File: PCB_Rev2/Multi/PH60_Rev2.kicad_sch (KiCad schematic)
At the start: 28 parts, among them J1 USB_C_Receptacle_USB2.0_16P, J2 Conn_01x02, U1 TLV1117-33, U2 W25Q128JVS, U3 RP2040, Y1 Crystal_GND24

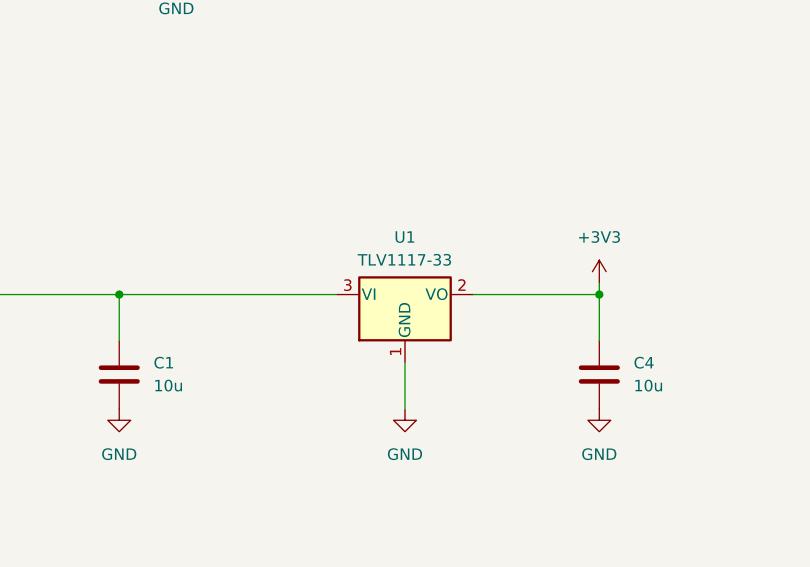
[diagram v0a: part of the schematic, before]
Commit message: LDO Modification
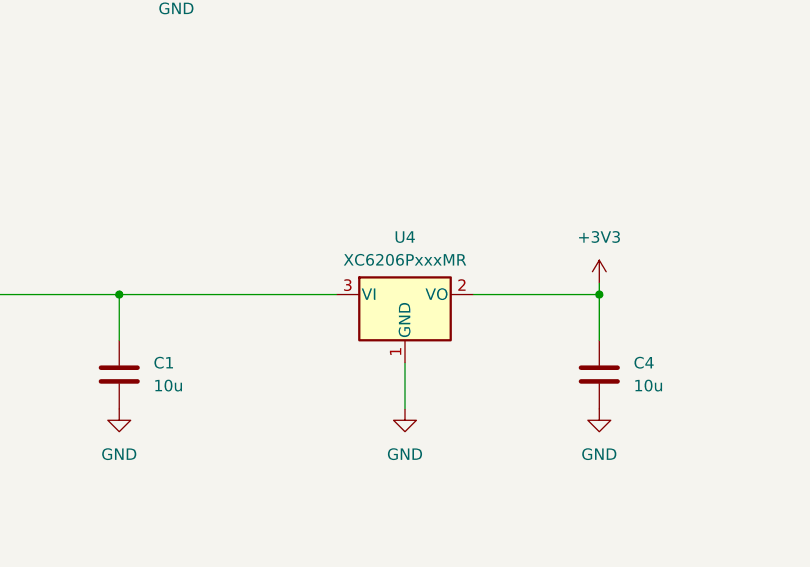
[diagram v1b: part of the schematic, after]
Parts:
- removed U1: TLV1117-33, Package_TO_SOT_SMD:SOT-89-3_Handsoldering, symbol Regulator_Linear:TLV1117-33
- added U4: XC6206PxxxMR, Package_TO_SOT_SMD:SOT-23-3, symbol Regulator_Linear:XC6206PxxxMR
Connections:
- net +3V3: now also U4.2 (VO)
- net GND: now also U4.1 (GND)
- net VBUS: now also U4.3 (VI)
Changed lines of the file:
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@@
-	)
-	(symbol
-		(lib_id "Regulator_Linear:TLV1117-33")
-		(at 134.62 196.85 0)
-		(unit 1)
-		(exclude_from_sim no)
-		(in_bom yes)
-		(on_board yes)
-		(dnp no)
-		(fields_autoplaced yes)
-		(property "Reference" "U1"
-			(at 134.62 190.5 0)
-			(effects
-				(font
-					(size 1.27 1.27)
-				)
-			)
-		)
-		(property "Value" "TLV1117-33"
-			(at 134.62 193.04 0)
-			(effects
-				(font
-					(size 1.27 1.27)
-				)
-			)
-		)
-		(property "Footprint" "Package_TO_SOT_SMD:SOT-89-3_Handsoldering"
-			(at 134.62 196.85 0)
-			(effects
-				(font
-					(size 1.27 1.27)
-				)
-				(hide yes)
-			)
-		)
-		(property "Datasheet" "http://www.ti.com/lit/ds/symlink/tlv1117.pdf"
-			(at 134.62 196.85 0)
-			(effects
-				(font
-					(size 1.27 1.27)
-				)
-				(hide yes)
-			)
-		)
-		(property "Description" "800mA Low-Dropout Linear Regulator, 3.3V fixed output, TO-220/TO-252/TO-263/SOT-223"
-			(at 134.62 196.85 0)
-			(effects
-				(font
-					(size 1.27 1.27)
-				)
-				(hide yes)
-			)
-		)
-		(pin "3"
-		)
-		(pin "1"
-		)
-		(pin "2"
-		)
-		(instances
-			(project ""
-				(path "/dca0f898-8fdb-4522-a51d-f4f4238906e7"
-					(reference "U1")
-					(unit 1)
-				)
-			)
-		)
 	)
 	(symbol
@@
 	)
 	(symbol
+		(lib_id "Regulator_Linear:XC6206PxxxMR")
+		(at 134.62 196.85 0)
+		(unit 1)
+		(exclude_from_sim no)
+		(in_bom yes)
+		(on_board yes)
+		(dnp no)
+		(fields_autoplaced yes)
+		(property "Reference" "U4"
+			(at 134.62 190.5 0)
+			(effects
+				(font
+					(size 1.27 1.27)
+				)
+			)
+		)
+		(property "Value" "XC6206PxxxMR"
+			(at 134.62 193.04 0)
+			(effects
+				(font
+					(size 1.27 1.27)
+				)
+			)
+		)
+		(property "Footprint" "Package_TO_SOT_SMD:SOT-23-3"
+			(at 134.62 191.135 0)
+			(effects
+				(font
+					(size 1.27 1.27)
+					(italic yes)
+				)
+				(hide yes)
+			)
+		)
+		(property "Datasheet" "https://www.torexsemi.com/file/xc6206/XC6206.pdf"
+			(at 134.62 196.85 0)
+			(effects
+				(font
+					(size 1.27 1.27)
+				)
+				(hide yes)
+			)
+		)
+		(property "Description" "Positive 60-250mA Low Dropout Regulator, Fixed Output, SOT-23"
+			(at 134.62 196.85 0)
+			(effects
+				(font
+					(size 1.27 1.27)
+				)
+				(hide yes)
+			)
+		)
+		(pin "3"
+		)
+		(pin "1"
+		)
+		(pin "2"
+		)
+		(instances
+			(project ""
+				(path "/dca0f898-8fdb-4522-a51d-f4f4238906e7"
+					(reference "U4")
+					(unit 1)
+				)
+			)
+		)
+	)
+	(symbol
 		(lib_id "power:GND")
 		(at 83.82 48.26 0)
@@
 		)
 		(instances
-			(project "PH60_Rev3"
+			(project "PH60_Rev2"
 				(path "/dca0f898-8fdb-4522-a51d-f4f4238906e7"
 					(page "2")

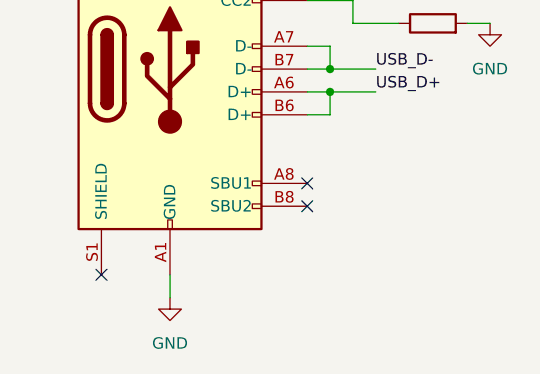
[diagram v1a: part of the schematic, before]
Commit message: Add GH60 Mounting
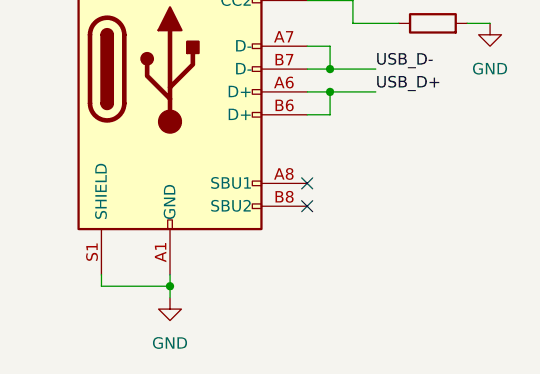
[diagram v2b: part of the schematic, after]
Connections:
- net GND: now also J1.S1 (SHIELD)
- no-connect marks 17 -> 16
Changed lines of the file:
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@@
+	)
+	(junction
+		(at 48.26 245.11)
+		(diameter 0)
+		(color 0 0 0 0)
 	)
 	(junction
@@
 	)
 	(no_connect
-		(at 40.64 243.84)
-	)
-	(no_connect
 		(at 134.62 129.54)
 	)
@@
 	(wire
 		(pts
+			(xy 40.64 243.84) (xy 40.64 245.11)
+		)
+		(stroke
+			(width 0)
+			(type default)
+		)
+	)
+	(wire
+		(pts
 			(xy 67.31 104.14) (xy 83.82 104.14)
 		)
@@
 	(wire
 		(pts
+			(xy 40.64 245.11) (xy 48.26 245.11)
+		)
+		(stroke
+			(width 0)
+			(type default)
+		)
+	)
+	(wire
+		(pts
 			(xy 68.58 210.82) (xy 68.58 205.74)
 		)
@@
 	(wire
 		(pts
-			(xy 48.26 243.84) (xy 48.26 246.38)
-		)
-		(stroke
+			(xy 48.26 243.84) (xy 48.26 245.11)
+		)
+		(stroke
+			(width 0)
+			(type default)
+		)
+	)
+	(wire
+		(pts
+			(xy 48.26 245.11) (xy 48.26 246.38)
+		)
+		(stroke

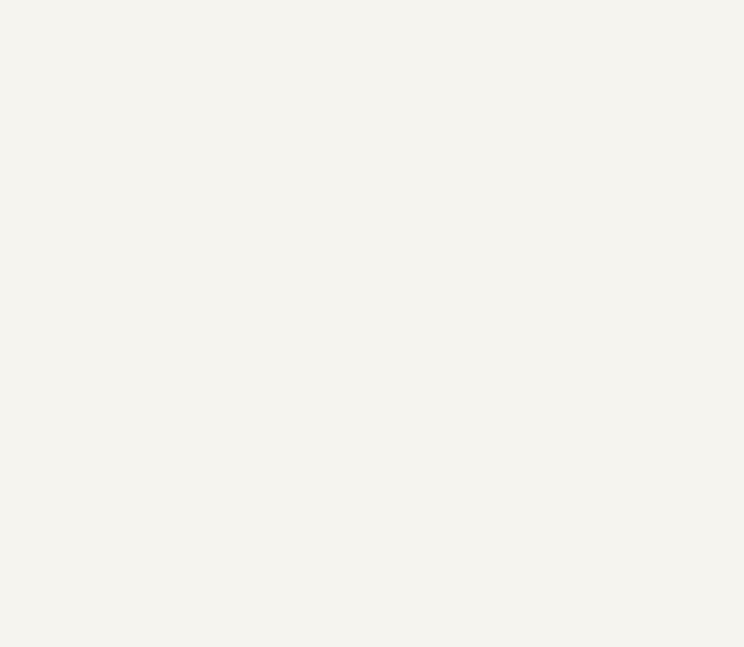
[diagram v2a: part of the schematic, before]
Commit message: Schematic Tinkering and RF Module Placing
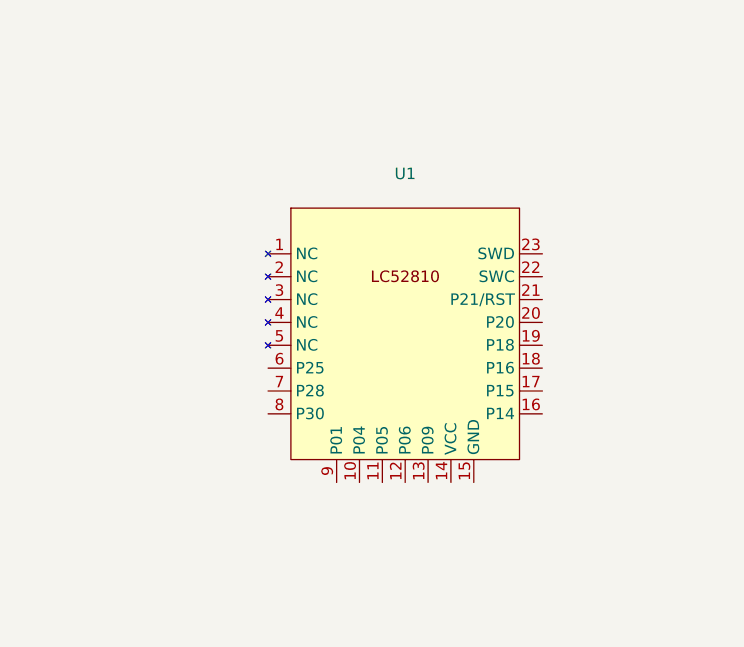
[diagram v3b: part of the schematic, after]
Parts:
- added U1: ~, nRF_Module:nRF52810_Module, symbol nRF52810_Module:LC52810
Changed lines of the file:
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@@
+	)
+	(symbol
+		(lib_id "nRF52810_Module:LC52810")
+		(at 350.52 151.13 0)
+		(unit 1)
+		(exclude_from_sim no)
+		(in_bom yes)
+		(on_board yes)
+		(dnp no)
+		(fields_autoplaced yes)
+		(property "Reference" "U1"
+			(at 350.52 142.24 0)
+			(effects
+				(font
+					(size 1.27 1.27)
+				)
+			)
+		)
+		(property "Value" "~"
+			(at 350.52 144.78 0)
+			(effects
+				(font
+					(size 1.27 1.27)
+				)
+			)
+		)
+		(property "Footprint" "nRF_Module:nRF52810_Module"
+			(at 350.52 151.13 0)
+			(effects
+				(font
+					(size 1.27 1.27)
+				)
+				(hide yes)
+			)
+		)
+		(property "Datasheet" ""
+			(at 350.52 151.13 0)
+			(effects
+				(font
+					(size 1.27 1.27)
+				)
+				(hide yes)
+			)
+		)
+		(property "Description" ""
+			(at 350.52 151.13 0)
+			(effects
+				(font
+					(size 1.27 1.27)
+				)
+				(hide yes)
+			)
+		)
+		(pin "11"
+		)
+		(pin "14"
+		)
+		(pin "15"
+		)
+		(pin "8"
+		)
+		(pin "6"
+		)
+		(pin "21"
+		)
+		(pin "9"
+		)
+		(pin "17"
+		)
+		(pin "10"
+		)
+		(pin "3"
+		)
+		(pin "22"
+		)
+		(pin "23"
+		)
+		(pin "1"
+		)
+		(pin "18"
+		)
+		(pin "5"
+		)
+		(pin "16"
+		)
+		(pin "2"
+		)
+		(pin "20"
+		)
+		(pin "7"
+		)
+		(pin "12"
+		)
+		(pin "19"
+		)
+		(pin "4"
+		)
+		(pin "13"
+		)
+		(instances
+			(project ""
+				(path "/dca0f898-8fdb-4522-a51d-f4f4238906e7"
+					(reference "U1")
+					(unit 1)
+				)
+			)
+		)
 	)
 	(symbol

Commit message: Multi PCB Rework
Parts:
- J2: footprint Connector_PinHeader_2.54mm:PinHeader_1x02_P2.54mm_Vertical -> Connector_PinHeader_1.27mm:PinHeader_1x02_P1.27mm_Vertical
- U1: now not fitted
- U2: footprint Package_SO:SOIC-8_5.23x5.23mm_P1.27mm -> Package_SON:Winbond_USON-8-1EP_3x2mm_P0.5mm_EP0.2x1.6mm
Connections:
- net row_2: now also U3.29 (GPIO18); no longer U3.27 (GPIO16)
- net row_3: now also U3.30 (GPIO19); no longer U3.28 (GPIO17)
- net row_4: now also U3.31 (GPIO20); no longer U3.29 (GPIO18)
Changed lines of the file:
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@@
 	)
 	(no_connect
+		(at 134.62 114.3)
+	)
+	(no_connect
 		(at 134.62 129.54)
 	)
@@
 	)
 	(no_connect
-		(at 134.62 121.92)
-	)
-	(no_connect
 		(at 134.62 144.78)
 	)
@@
 	)
 	(no_connect
-		(at 134.62 124.46)
+		(at 83.82 73.66)
 	)
 	(no_connect
-		(at 83.82 73.66)
+		(at 134.62 116.84)
 	)
 	(no_connect
@@
 	(global_label "row_2"
 		(shape input)
-		(at 134.62 114.3 0)
+		(at 134.62 119.38 0)
 		(fields_autoplaced yes)
 		(effects
@@
 		)
 		(property "Intersheetrefs" "${INTERSHEET_REFS}"
-			(at 143.048 114.3 0)
+			(at 143.048 119.38 0)
 			(effects
 				(font
@@
 	(global_label "row_3"
 		(shape input)
-		(at 134.62 116.84 0)
+		(at 134.62 121.92 0)
 		(fields_autoplaced yes)
 		(effects
@@
 		)
 		(property "Intersheetrefs" "${INTERSHEET_REFS}"
-			(at 143.048 116.84 0)
+			(at 143.048 121.92 0)
 			(effects
 				(font
@@
 	(global_label "row_4"
 		(shape input)
-		(at 134.62 119.38 0)
+		(at 134.62 124.46 0)
 		(fields_autoplaced yes)
 		(effects
@@
 		)
 		(property "Intersheetrefs" "${INTERSHEET_REFS}"
-			(at 143.048 119.38 0)
+			(at 143.048 124.46 0)
 			(effects
 				(font
@@
 			)
 		)
-		(property "Footprint" "Package_SO:SOIC-8_5.23x5.23mm_P1.27mm"
+		(property "Footprint" "Package_SON:Winbond_USON-8-1EP_3x2mm_P0.5mm_EP0.2x1.6mm"
 			(at 274.32 116.84 0)
 			(effects
@@
 		(exclude_from_sim no)
 		(in_bom yes)
-		(on_board yes)
-		(dnp no)
+		(on_board no)
+		(dnp yes)
 		(fields_autoplaced yes)
 		(property "Reference" "U1"
@@
 			)
 		)
-		(property "Footprint" "Connector_PinHeader_2.54mm:PinHeader_1x02_P2.54mm_Vertical"
+		(property "Footprint" "Connector_PinHeader_1.27mm:PinHeader_1x02_P1.27mm_Vertical"
 			(at 191.77 109.22 0)
 			(effects

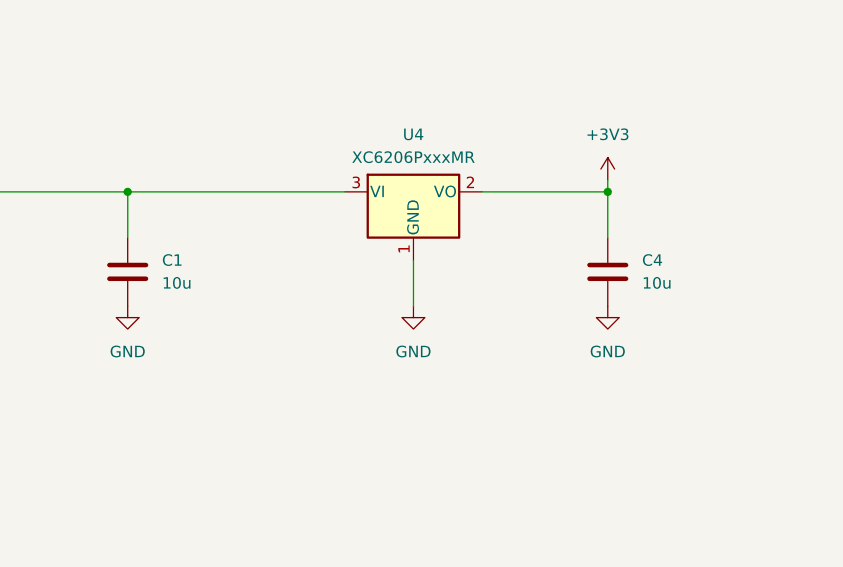
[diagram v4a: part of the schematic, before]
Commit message: Adjust the Capacitance of LDO Input/Output Capacitor
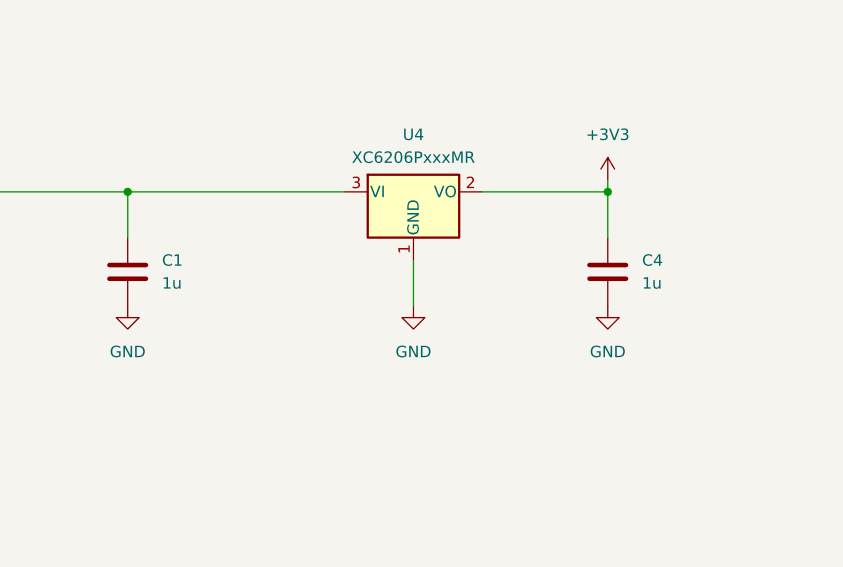
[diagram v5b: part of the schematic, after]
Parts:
- C1, C4: value 10u -> 1u
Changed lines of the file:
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@@
 			)
 		)
-		(property "Value" "10u"
+		(property "Value" "1u"
 			(at 160.02 207.0099 0)
 			(effects
@@
 			)
 		)
-		(property "Value" "10u"
+		(property "Value" "1u"
 			(at 106.68 207.0099 0)
 			(effects

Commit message: QFN-56 Thermal Via Redesign
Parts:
- U3: footprint Package_DFN_QFN:QFN-56-1EP_7x7mm_P0.4mm_EP3.2x3.2mm_ThermalVias -> Package_DFN_QFN:QFN-56-1EP_7x7mm_P0.4mm_EP3.2x3.2mm
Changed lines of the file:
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@@
 			)
 		)
-		(property "Footprint" "Package_DFN_QFN:QFN-56-1EP_7x7mm_P0.4mm_EP3.2x3.2mm_ThermalVias"
+		(property "Footprint" "Package_DFN_QFN:QFN-56-1EP_7x7mm_P0.4mm_EP3.2x3.2mm"
 			(at 109.22 111.76 0)
 			(effects

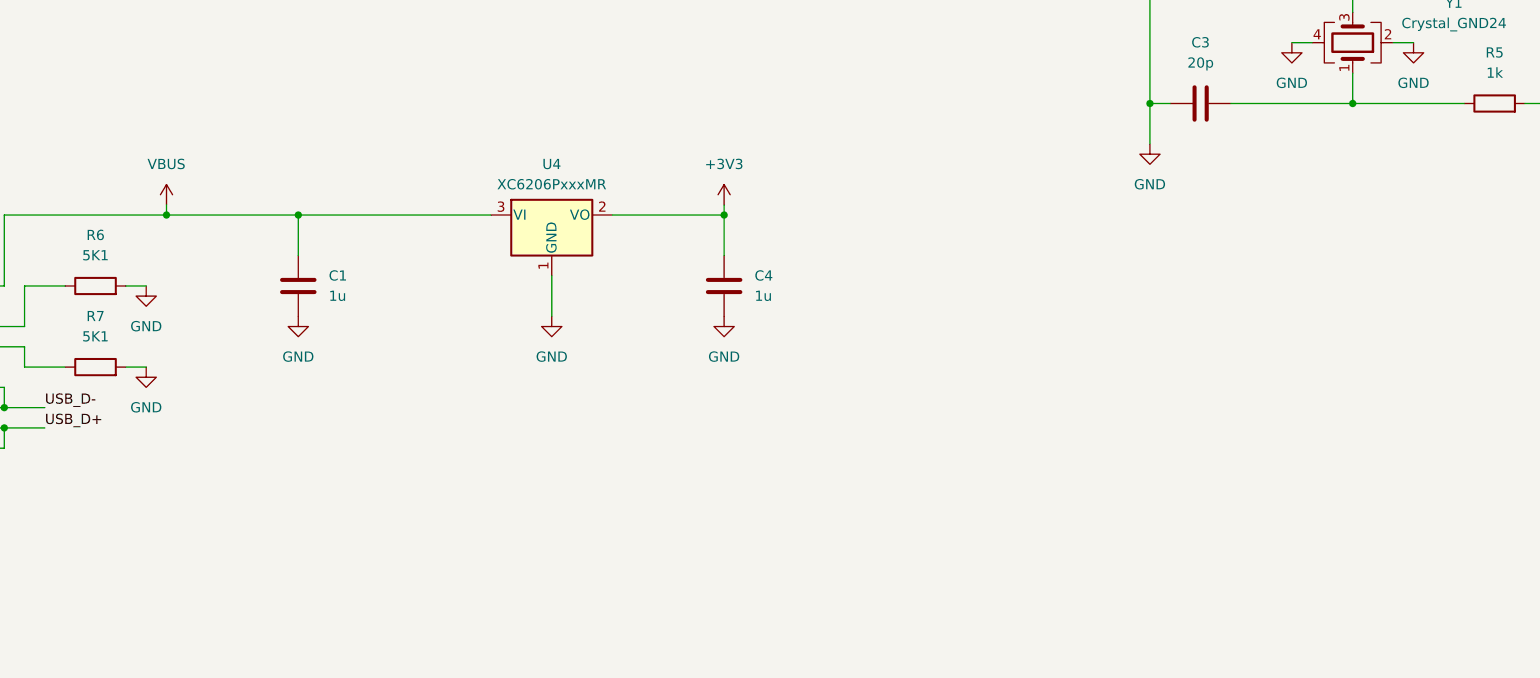
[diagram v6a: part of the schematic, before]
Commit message: Mounting hole improvement and ESD protection
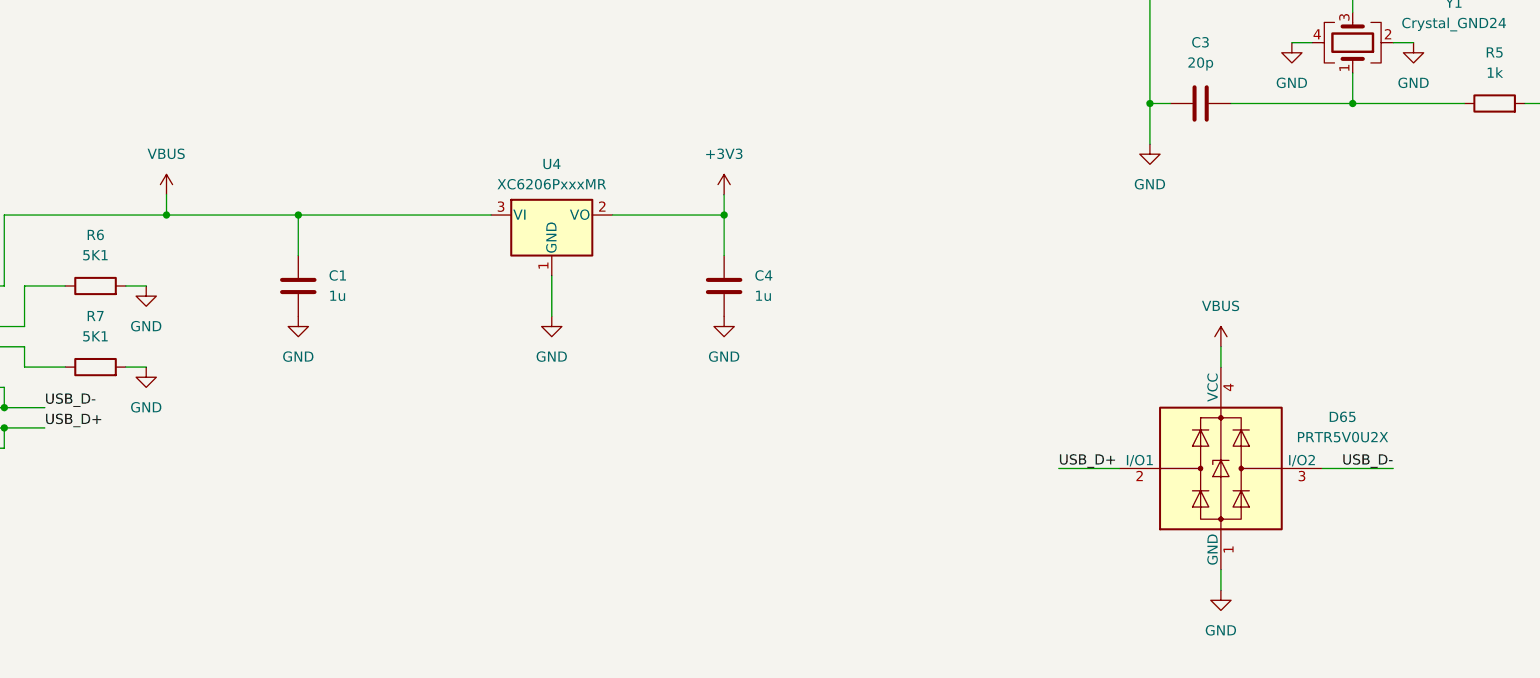
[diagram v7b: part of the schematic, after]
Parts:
- added D65: PRTR5V0U2X, Package_TO_SOT_SMD:SOT-143, symbol Power_Protection:PRTR5V0U2X
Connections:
- net GND: now also D65.1 (GND)
- net USB_D+: now also D65.2 (I/O1)
- net USB_D-: now also D65.3 (I/O2)
- net VBUS: now also D65.4 (VCC)

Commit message: Update PCB Routing
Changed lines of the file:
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@@
 (kicad_sch
-	(version 20231120)
+	(version 20250114)
 	(generator "eeschema")
-	(generator_version "8.0")
+	(generator_version "9.0")
 	(paper "A3")
 	(junction
@@
 		(at 332.74 34.29)
 		(size 53.34 27.94)
+		(exclude_from_sim no)
+		(in_bom yes)
+		(on_board yes)
+		(dnp no)
 		(fields_autoplaced yes)
 		(stroke
@@
 		)
 	)
+	(embedded_fonts no)
 )
